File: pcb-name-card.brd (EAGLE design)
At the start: 84 x 53 mm, 8 parts, among them U1 3V, U2 3V

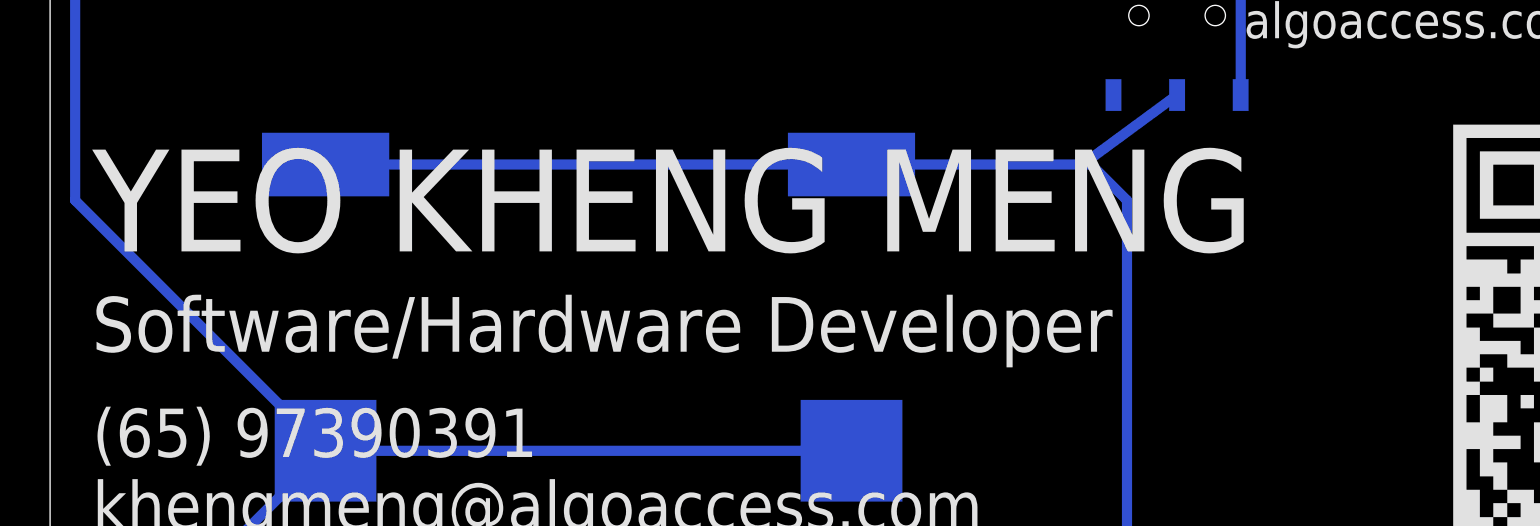
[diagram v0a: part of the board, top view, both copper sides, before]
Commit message: rev 3. one line on top layer so PCB manufacturers don't give me issue about missing top layer
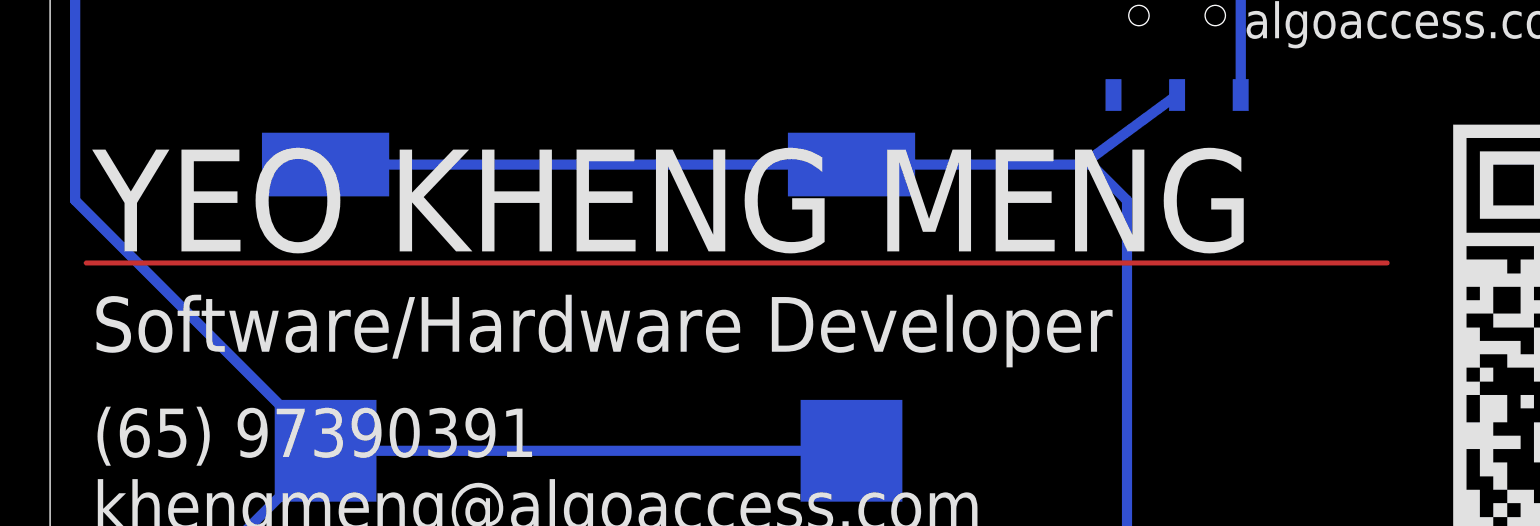
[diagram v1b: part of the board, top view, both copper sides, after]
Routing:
- net N$3: track 0.00 -> 52.0 mm
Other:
- board text added: "Rev 3"
- board text removed: "Rev 2"
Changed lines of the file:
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@@
 <setting verticaltext="up"/>
 </settings>
-<grid distance="1" unitdist="mm" unit="mm" style="lines" multiple="1" display="yes" altdistance="0.1" altunitdist="mm" altunit="mm"/>
+<grid distance="1" unitdist="mm" unit="mm" style="lines" multiple="1" display="yes" altdistance="0.01" altunitdist="mm" altunit="mm"/>
 <layers>
 <layer number="1" name="Top" color="4" fill="1" visible="yes" active="yes"/>
@@
 before toggling the switches</text>
 <text x="27.5" y="38.06" size="1.016" layer="22" font="vector" rot="MR0">CR2025/CR2016</text>
-<text x="23.21" y="18.06" size="0.8128" layer="22" font="vector" rot="MR0">Rev 2</text>
+<text x="23.21" y="18.06" size="0.8128" layer="22" font="vector" rot="MR0">Rev 3</text>
 <text x="47.671403125" y="42.473115625" size="1.4224" layer="21" font="vector">algoaccess.com</text>
 <rectangle x1="55.9391" y1="44.3959" x2="56.0915" y2="44.4213" layer="21"/>
@@
 <wire x1="43" y1="15.596178125" x2="42.001096875" y2="14.597275" width="0.4064" layer="16"/>
 </signal>
+<signal name="N$3">
+<wire x1="1.44" y1="33.5" x2="53.39" y2="33.5" width="0.2" layer="1"/>
+</signal>
 </signals>

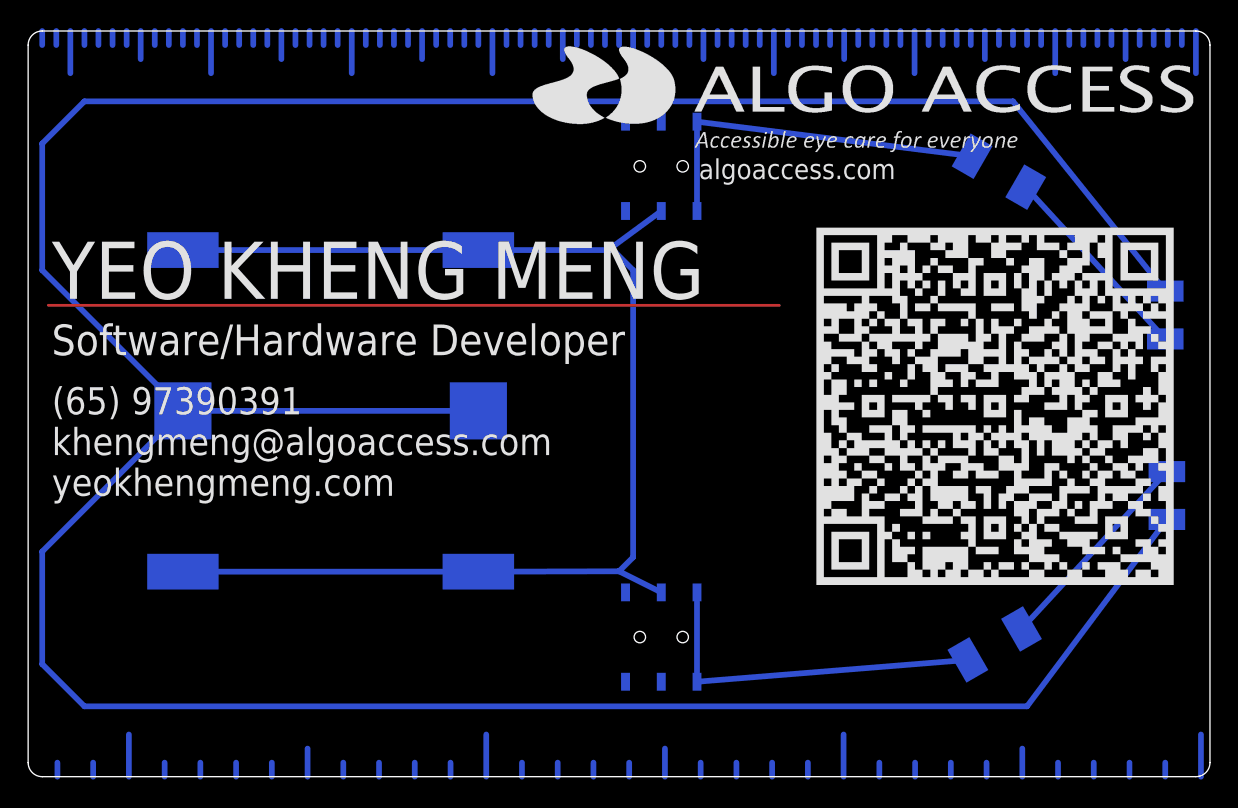
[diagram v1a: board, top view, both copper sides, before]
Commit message: larger positive battery contacts
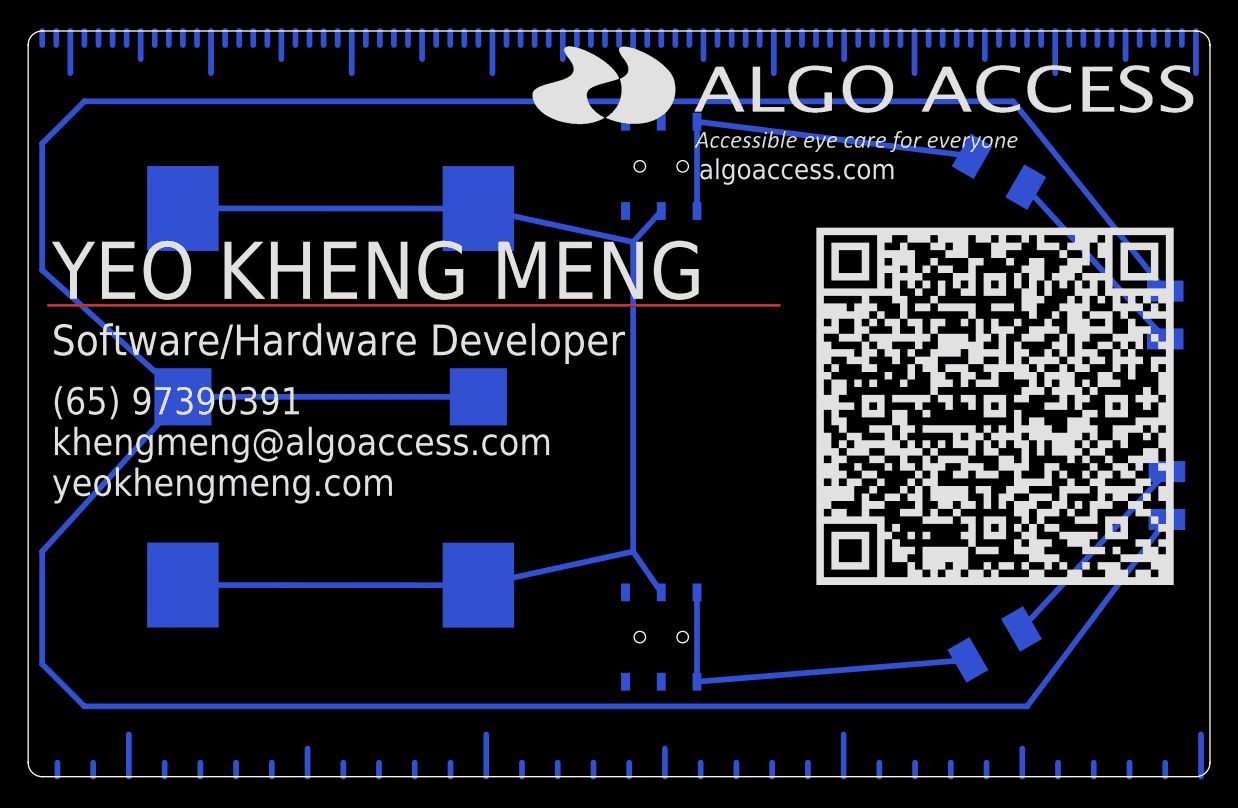
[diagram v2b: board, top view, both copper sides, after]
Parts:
- U1, U2: device cr2032:CR2032-SMD -> cr2032-large-side:CR2032-SMD
- moved U1 1.00 mm to (11.0, 27.0)
- moved U2 1.00 mm to (32.0, 27.0)
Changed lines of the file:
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@@
 <setting verticaltext="up"/>
 </settings>
-<grid distance="1" unitdist="mm" unit="mm" style="lines" multiple="1" display="yes" altdistance="0.01" altunitdist="mm" altunit="mm"/>
+<grid distance="1" unitdist="mm" unit="mm" style="lines" multiple="1" display="yes" altdistance="0.1" altunitdist="mm" altunit="mm"/>
 <layers>
 <layer number="1" name="Top" color="4" fill="1" visible="yes" active="yes"/>
@@
 <text x="49.771078125" y="39.7722" size="1.016" layer="22" font="vector" rot="MR270">Caution: Look away from LEDs
 before toggling the switches</text>
-<text x="27.5" y="38.06" size="1.016" layer="22" font="vector" rot="MR0">CR2025/CR2016</text>
-<text x="23.21" y="18.06" size="0.8128" layer="22" font="vector" rot="MR0">Rev 3</text>
+<text x="27.5" y="39.06" size="1.016" layer="22" font="vector" rot="MR0">CR2025/CR2016</text>
+<text x="23.21" y="19.06" size="0.8128" layer="22" font="vector" rot="MR0">Rev 3</text>
 <text x="47.671403125" y="42.473115625" size="1.4224" layer="21" font="vector">algoaccess.com</text>
 <rectangle x1="55.9391" y1="44.3959" x2="56.0915" y2="44.4213" layer="21"/>
@@
 <attribute name="COLOR" value="yellow" x="80.82315" y="32.81365" size="1.778" layer="28" rot="MR180" display="off"/>
 </element>
-<element name="U2" library="cr2032" package="CR2032-SMD" value="3V" x="32" y="26" smashed="yes" rot="MR90"/>
+<element name="U2" library="cr2032-large-side" package="CR2032-SMD" value="3V" x="32" y="27" smashed="yes" rot="MR90"/>
 <element name="SW1" library="Seeed-OPL-Switch" package="SW6-2.54-SMD-7.0X3.5X1.5MM" value="" x="45" y="43.380309375" smashed="yes" rot="MR90">
 <attribute name="MPN" value="MS-22C01" x="45" y="43.380309375" size="1.778" layer="28" rot="MR90" display="off"/>
@@
 <attribute name="COLOR" value="yellow" x="80.938" y="19.9834" size="1.778" layer="28" rot="MR0" display="off"/>
 </element>
-<element name="U1" library="cr2032" package="CR2032-SMD" value="3V" x="11" y="26" smashed="yes" rot="MR270"/>
+<element name="U1" library="cr2032-large-side" package="CR2032-SMD" value="3V" x="11" y="27" smashed="yes" rot="MR270"/>
 <element name="R1" library="resistor" package="R2010" value="10 ohm" x="69" y="43" smashed="yes" rot="MR210"/>
 <element name="R2" library="resistor" package="R2010" value="330 ohm" x="68.7" y="9.4" smashed="yes" rot="MR150"/>
@@
 <contactref element="LED2" pad="C"/>
 <contactref element="LED1" pad="C"/>
-<wire x1="11" y1="26" x2="32" y2="26" width="0.4064" layer="16"/>
-<wire x1="31.241221875" y1="26" x2="32" y2="26" width="0.4064" layer="16"/>
+<wire x1="11" y1="27" x2="32" y2="27" width="0.4064" layer="16"/>
+<wire x1="31.241221875" y1="27" x2="32" y2="27" width="0.4064" layer="16"/>
 <wire x1="80.938" y1="18.2834" x2="71" y2="5" width="0.4064" layer="16"/>
 <wire x1="71" y1="5" x2="4" y2="5" width="0.4064" layer="16"/>
 <wire x1="4" y1="5" x2="1" y2="8" width="0.4064" layer="16"/>
 <wire x1="1" y1="8" x2="1" y2="16" width="0.4064" layer="16"/>
-<wire x1="1" y1="16" x2="11" y2="26" width="0.4064" layer="16"/>
+<wire x1="1" y1="16" x2="11" y2="27" width="0.4064" layer="16"/>
 <wire x1="80.82315" y1="34.51365" x2="70" y2="48" width="0.4064" layer="16"/>
 <wire x1="70" y1="48" x2="4" y2="48" width="0.4064" layer="16"/>
 <wire x1="4" y1="48" x2="1" y2="45" width="0.4064" layer="16"/>
 <wire x1="1" y1="45" x2="1" y2="36" width="0.4064" layer="16"/>
-<wire x1="1" y1="36" x2="11" y2="26" width="0.4064" layer="16"/>
+<wire x1="1" y1="36" x2="11" y2="27" width="0.4064" layer="16"/>
 </signal>
 <signal name="N$9">
@@
 <contactref element="U2" pad="+$2"/>
 <contactref element="SW1" pad="COM1"/>
-<wire x1="11" y1="37.43" x2="32" y2="37.43" width="0.4064" layer="16"/>
-<wire x1="11" y1="14.57" x2="32" y2="14.57" width="0.4064" layer="16"/>
-<wire x1="32" y1="14.57" x2="42.001096875" y2="14.597275" width="0.4064" layer="16"/>
-<wire x1="42.001096875" y1="14.597275" x2="42" y2="14.6" width="0.4064" layer="16"/>
-<wire x1="42" y1="14.6" x2="45" y2="13.0979125" width="0.4064" layer="16"/>
-<wire x1="41.224690625" y1="37.43" x2="45" y2="40.205309375" width="0.4064" layer="16"/>
-<wire x1="32" y1="37.43" x2="41.224690625" y2="37.43" width="0.4064" layer="16"/>
-<wire x1="41.224690625" y1="37.43" x2="41.57" y2="37.43" width="0.4064" layer="16"/>
-<wire x1="41.57" y1="37.43" x2="43" y2="36" width="0.4064" layer="16"/>
-<wire x1="43" y1="36" x2="43" y2="15.596178125" width="0.4064" layer="16"/>
-<wire x1="43" y1="15.596178125" x2="42.001096875" y2="14.597275" width="0.4064" layer="16"/>
+<wire x1="11" y1="40.39" x2="32" y2="40.38" width="0.4064" layer="16"/>
+<wire x1="11" y1="13.62" x2="32" y2="13.61" width="0.4064" layer="16"/>
+<wire x1="32" y1="40.38" x2="43" y2="38" width="0.4064" layer="16"/>
+<wire x1="43" y1="38" x2="43" y2="16" width="0.4064" layer="16"/>
+<wire x1="43" y1="16" x2="32" y2="13.61" width="0.4064" layer="16"/>
+<wire x1="45" y1="13.0979125" x2="43" y2="16" width="0.4064" layer="16"/>
+<wire x1="45" y1="40.205309375" x2="43" y2="38" width="0.4064" layer="16"/>
 </signal>
 <signal name="N$3">
